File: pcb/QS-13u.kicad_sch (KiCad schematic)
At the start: 98 parts, among them J1 Conn_01x04, J2 USB_C_Receptacle_USB2.0, SW1 MX_SW_solder, SW10 MX_SW_solder, SW11 MX_SW_solder, SW12 MX_SW_solder, SW13 MX_SW_solder, SW14 MX_SW_solder, SW15 MX_SW_solder, SW16 MX_SW_solder, SW17 MX_SW_solder, SW18 MX_SW_solder, SW19 MX_SW_solder, SW2 MX_SW_solder, SW20 MX_SW_solder, SW21 MX_SW_solder, SW22 MX_SW_solder, SW23 MX_SW_solder, SW24 MX_SW_solder, SW25 MX_SW_solder, SW26 MX_SW_solder, SW27 MX_SW_solder, SW28 MX_SW_solder, SW29 MX_SW_solder, SW3 MX_SW_solder, SW30 MX_SW_solder, SW31 MX_SW_solder, SW32 MX_SW_solder, SW33 MX_SW_solder, SW34 MX_SW_solder, SW35 MX_SW_solder, SW36 MX_SW_solder, SW37 MX_SW_solder, SW38 MX_SW_solder, SW39 MX_SW_solder, SW4 MX_SW_solder, SW40 MX_SW_solder, SW41 MX_SW_solder, SW42 MX_SW_solder, SW43 MX_SW_solder, SW44 MX_SW_solder, SW45 MX_SW_solder, SW46 MX_SW_solder, SW47 MX_SW_solder, SW48 MX_SW_solder, SW49 MX_SW_solder, SW5 MX_SW_solder, SW50 MX_SW_solder, SW51 MX_SW_solder, SW52 MX_SW_solder, SW53 MX_SW_solder, SW54 MX_SW_solder, SW55 SW_Push, SW6 MX_SW_solder, SW7 MX_SW_solder, SW8 MX_SW_solder, SW9 MX_SW_solder, U1 USBLC6-2SC6, U2 ATmega32U2-M, Y1 16 MHz

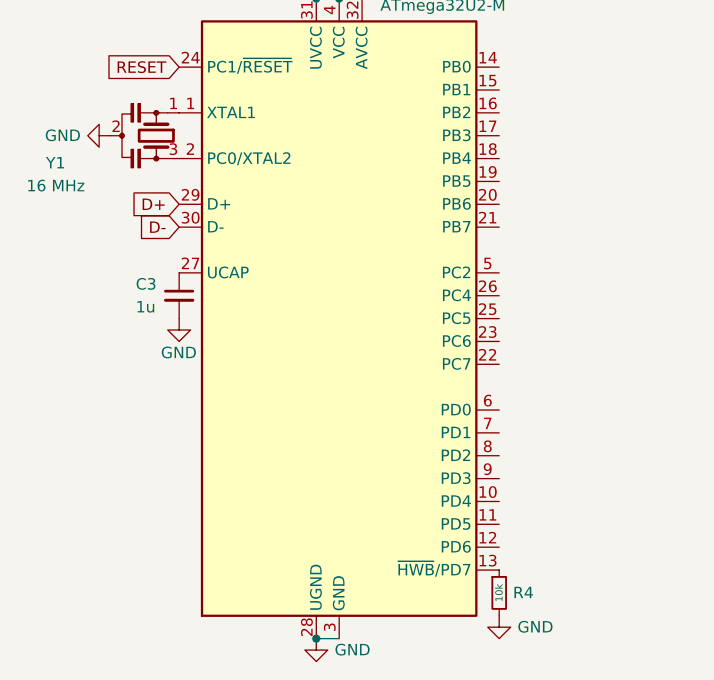
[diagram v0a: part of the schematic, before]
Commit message: Fixes + Updates
- Fixed some weird submodules shenanigans
- Repositioned the JST connector
- Adjusted the outline for gummy o-ring mount
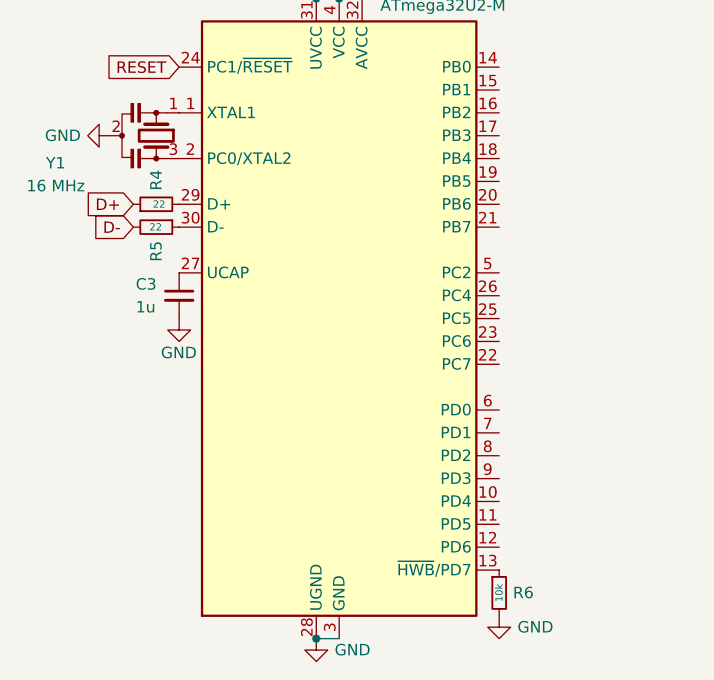
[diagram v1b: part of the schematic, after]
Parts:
- added R4, R5: 22, Resistor_SMD:R_0603_1608Metric, symbol Device:R_Small
- renumbered R4 to R6
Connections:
- net D+: now also R4.1; no longer U2.29 (D+)
- net D-: now also R5.2; no longer U2.30 (D-)
- new net: R4.2, U2.29 (D+)
- new net: R5.1, U2.30 (D-)
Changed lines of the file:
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@@
     )
   )
-  (global_label "D+" (shape input) (at 34.036 141.986 180) (fields_autoplaced)
+  (global_label "D+" (shape input) (at 28.956 141.986 180) (fields_autoplaced)
     (effects (font (size 1.27 1.27)) (justify right))
-    (property "Intersheet References" "${INTERSHEET_REFS}" (id 0) (at 28.7805 141.9066 0)
+    (property "Intersheet References" "${INTERSHEET_REFS}" (id 0) (at 23.7005 141.9066 0)
       (effects (font (size 1.27 1.27)) (justify right) hide)
     )
@@
     )
   )
-  (global_label "D-" (shape input) (at 34.036 144.526 180) (fields_autoplaced)
+  (global_label "D-" (shape input) (at 28.956 144.526 180) (fields_autoplaced)
     (effects (font (size 1.27 1.27)) (justify right))
-    (property "Intersheet References" "${INTERSHEET_REFS}" (id 0) (at 28.7805 144.4466 0)
+    (property "Intersheet References" "${INTERSHEET_REFS}" (id 0) (at 23.7005 144.4466 0)
       (effects (font (size 1.27 1.27)) (justify right) hide)
     )
@@
     (pin "2")
   )
+  (symbol (lib_id "Device:R_Small") (at 31.496 144.526 270) (unit 1)
+    (in_bom yes) (on_board yes)
+    (property "Reference" "R5" (id 0) (at 31.496 146.05 0)
+      (effects (font (size 1.27 1.27)) (justify left))
+    )
+    (property "Value" "22" (id 1) (at 30.734 144.526 90)
+      (effects (font (size 0.8 0.8)) (justify left))
+    )
+    (property "Footprint" "Resistor_SMD:R_0603_1608Metric" (id 2) (at 31.496 144.526 0)
+      (effects (font (size 1.27 1.27)) hide)
+    )
+    (property "Datasheet" "~" (id 3) (at 31.496 144.526 0)
+      (effects (font (size 1.27 1.27)) hide)
+    )
+    (pin "1")
+    (pin "2")
+  )
   (symbol (lib_id "power:+5V") (at 52.07 85.598 0) (unit 1)
     (in_bom yes) (on_board yes) (fields_autoplaced)
@@
     )
     (pin "1")
+  )
+  (symbol (lib_id "Device:R_Small") (at 31.496 141.986 90) (unit 1)
+    (in_bom yes) (on_board yes)
+    (property "Reference" "R4" (id 0) (at 31.496 140.462 0)
+      (effects (font (size 1.27 1.27)) (justify left))
+    )
+    (property "Value" "22" (id 1) (at 32.512 141.986 90)
+      (effects (font (size 0.8 0.8)) (justify left))
+    )
+    (property "Footprint" "Resistor_SMD:R_0603_1608Metric" (id 2) (at 31.496 141.986 0)
+      (effects (font (size 1.27 1.27)) hide)
+    )
+    (property "Datasheet" "~" (id 3) (at 31.496 141.986 0)
+      (effects (font (size 1.27 1.27)) hide)
+    )
+    (pin "1")
+    (pin "2")
   )
   (symbol (lib_id "marbastlib-mx:MX_SW_solder") (at 83.82 51.308 0) (unit 1)
@@
   (symbol (lib_id "Device:R_Small") (at 69.596 185.166 0) (unit 1)
     (in_bom yes) (on_board yes)
-    (property "Reference" "R4" (id 0) (at 71.12 185.166 0)
+    (property "Reference" "R6" (id 0) (at 71.12 185.166 0)
       (effects (font (size 1.27 1.27)) (justify left))
     )
@@
       (reference "R3") (unit 1) (value "10k") (footprint "Resistor_SMD:R_0603_1608Metric")
     )
+    (path "/63e7494d-b1cf-4811-976d-8b9b2686c05e"
+      (reference "R4") (unit 1) (value "22") (footprint "Resistor_SMD:R_0603_1608Metric")
+    )
+    (path "/14d7bab6-83eb-4766-b047-d59aead7750f"
+      (reference "R5") (unit 1) (value "22") (footprint "Resistor_SMD:R_0603_1608Metric")
+    )
     (path "/74f7faf4-f39c-4226-b601-5341f12f2216"
-      (reference "R4") (unit 1) (value "10k") (footprint "Resistor_SMD:R_0603_1608Metric")
+      (reference "R6") (unit 1) (value "10k") (footprint "Resistor_SMD:R_0603_1608Metric")
     )
     (path "/6dd7bde8-412d-40cb-95e0-7d7ac01fa232"

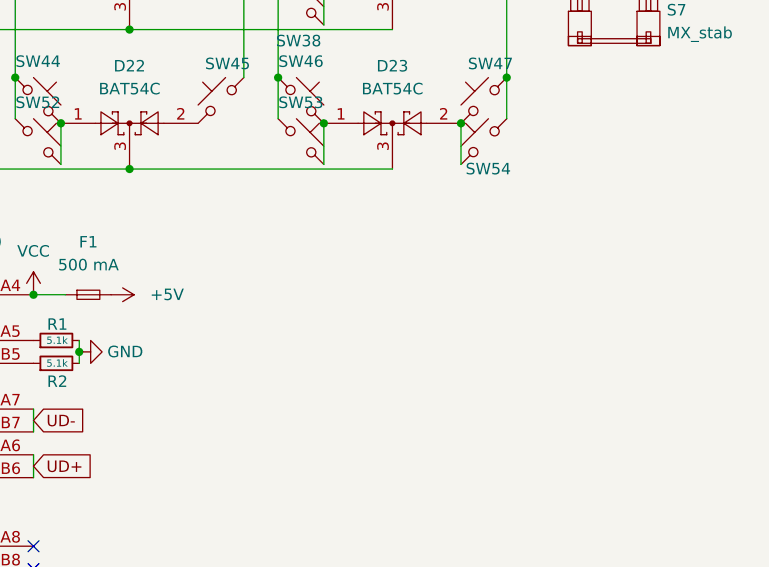
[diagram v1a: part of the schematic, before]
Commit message: USB Port + DB Routed
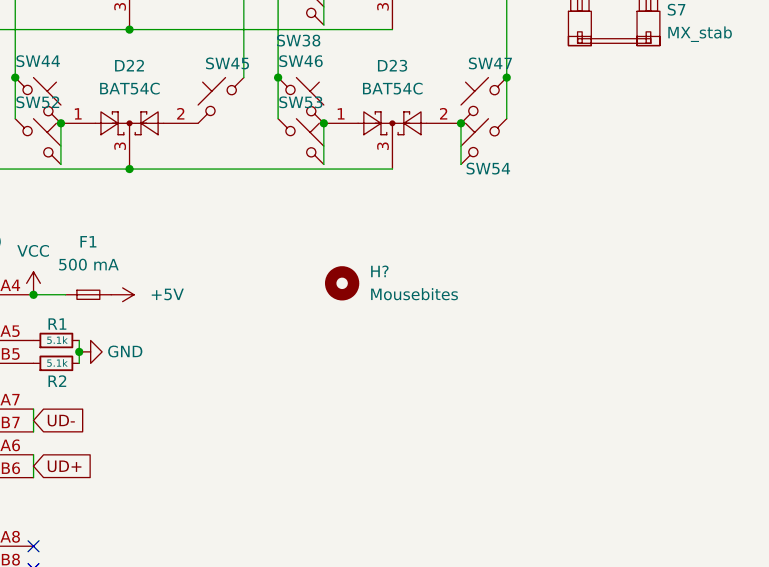
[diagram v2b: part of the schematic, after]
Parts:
- added H?: Mousebites, symbol Mechanical:MountingHole
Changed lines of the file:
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@@
     (pin "3")
+  )
+  (symbol (lib_id "Mechanical:MountingHole") (at 176.022 87.122 0) (unit 1)
+    (in_bom yes) (on_board yes) (fields_autoplaced)
+    (property "Reference" "H?" (id 0) (at 179.07 85.8519 0)
+      (effects (font (size 1.27 1.27)) (justify left))
+    )
+    (property "Value" "Mousebites" (id 1) (at 179.07 88.3919 0)
+      (effects (font (size 1.27 1.27)) (justify left))
+    )
+    (property "Footprint" "" (id 2) (at 176.022 87.122 0)
+      (effects (font (size 1.27 1.27)) hide)
+    )
+    (property "Datasheet" "~" (id 3) (at 176.022 87.122 0)
+      (effects (font (size 1.27 1.27)) hide)
+    )
   )
   (symbol (lib_id "marbastlib-mx:MX_SW_solder") (at 113.03 35.814 0) (unit 1)
@@
       (reference "F1") (unit 1) (value "500 mA") (footprint "Fuse:Fuse_1206_3216Metric")
     )
+    (path "/25078e17-4edd-45a9-af7c-a97ed2e0179d"
+      (reference "H?") (unit 1) (value "Mousebites") (footprint "")
+    )
     (path "/8eb4900f-e62d-4ef3-9cee-326f89c9cbbb"

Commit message: PCB Rev.1
Everything seems to be connected and no obvious errors were found
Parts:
- gave numbers to parts that had none: 1
- renumbered SW55 to RESET1
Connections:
- net GND: now also J2.S1 (SHIELD)
- net COL7: now reaches U2.10 (PD4)
- net COL7: now also SW21.2, SW33.2, SW8.2
- net COL6: now reaches U2.11 (PD5)
- net COL6: now also SW20.1, SW32.1, SW7.1
- net COL3: now reaches U2.12 (PD6)
- net COL3: now also SW17.2, SW29.2, SW4.2
- net ROW1: now reaches U2.14 (PB0)
- net ROW1: now also D13.3, D14.3, D15.3, D16.3, D17.3, D18.3
- net COL8: now reaches U2.15 (PB1)
- net COL8: now also SW22.1, SW34.1, SW44.1, SW52.1, SW9.1
- net COL5: now reaches U2.16 (PB2)
- net COL5: now also SW19.2, SW31.2, SW43.2, SW51.2, SW6.2
- net COL4: now reaches U2.17 (PB3)
- net COL4: now also SW18.1, SW30.1, SW42.1, SW5.1, SW50.1
- net COL2: now reaches U2.18 (PB4)
- net COL2: now also SW16.1, SW28.1, SW3.1, SW41.1, SW49.1
- net COL1: now reaches U2.19 (PB5)
- net COL1: now also SW15.2, SW2.2, SW27.2, SW40.2
- net ROW0: now reaches U2.20 (PB6)
- net ROW0: now also D19.3, D20.3, D21.3, D22.3, D23.3
- net COL0: now reaches U2.23 (PC6)
- net COL0: now also SW1.1, SW14.1, SW26.1, SW39.1, SW48.1
- net ROW3: now reaches U2.25 (PC5)
- net ROW3: now also D1.3, D2.3, D3.3, D4.3, D5.3, D6.3
- net ROW2: now reaches U2.6 (PD0)
- net ROW2: now also D10.3, D11.3, D12.3, D7.3, D8.3, D9.3
- net COL11: now reaches U2.7 (PD1)
- net COL11: now also SW12.2, SW13.2, SW25.2, SW37.2, SW47.2, SW54.2
- net COL10: now reaches U2.8 (PD2)
- net COL10: now also SW11.1, SW24.1, SW36.1, SW38.1, SW46.1, SW53.1
- net COL9: now reaches U2.9 (PD3)
- net COL9: now also SW10.2, SW23.2, SW35.2, SW45.2
- net at SW14.2: now also D7.2; no longer D7.1
- net at SW15.1: now also D7.1; no longer D7.2
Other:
- moved on the sheet: C1, C2, D1, D10, D11, D12, D13, D14, D15, D16, D17, D18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
